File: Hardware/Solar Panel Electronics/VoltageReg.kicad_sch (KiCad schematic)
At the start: 22 parts, among them J14 Screw_Terminal_5VRail, Q2 Q_NMOS_DGS, Q3 Q_NMOS_DGS, U6 LM5118MH, U7 LT1963AxST-3.3

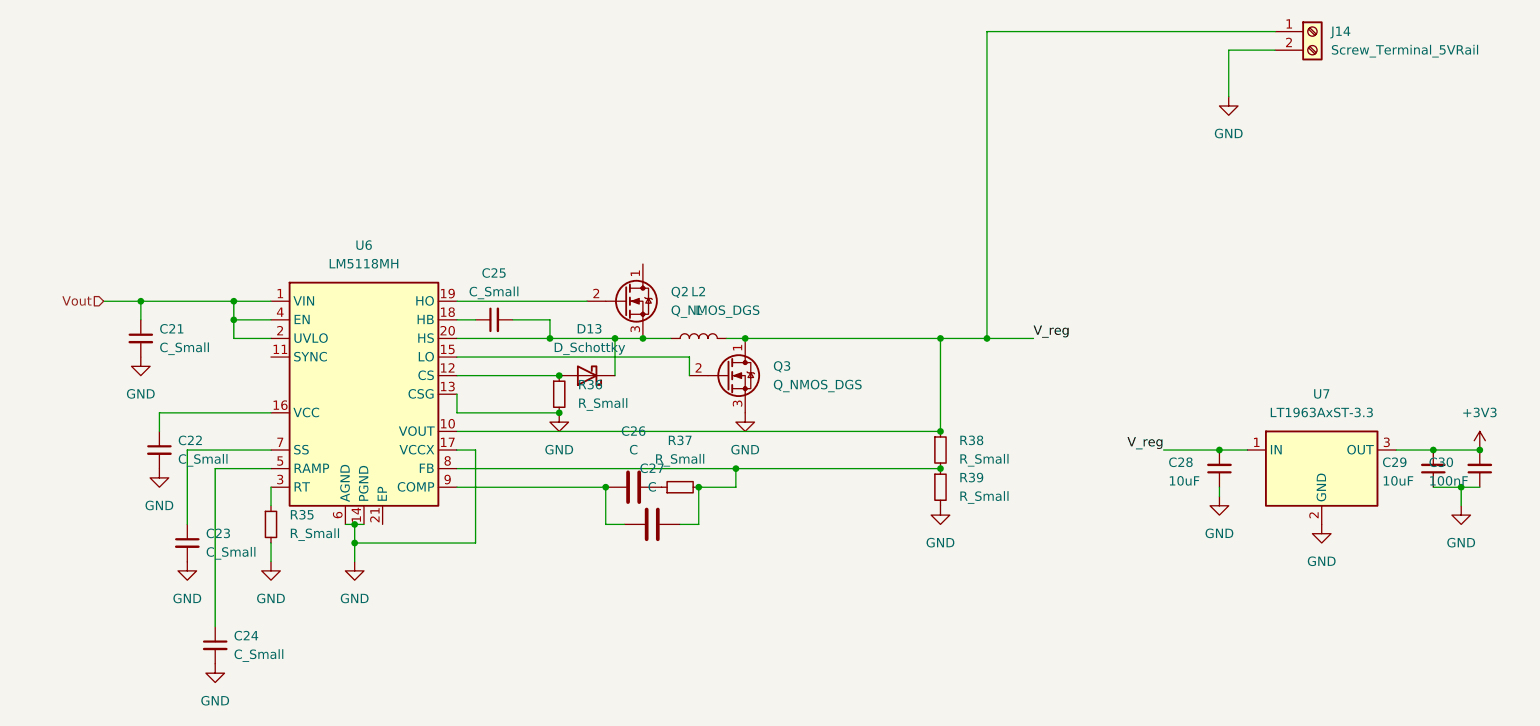
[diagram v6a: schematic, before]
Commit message: Sized the buck-boost converter components. Need to complete pcb layout.
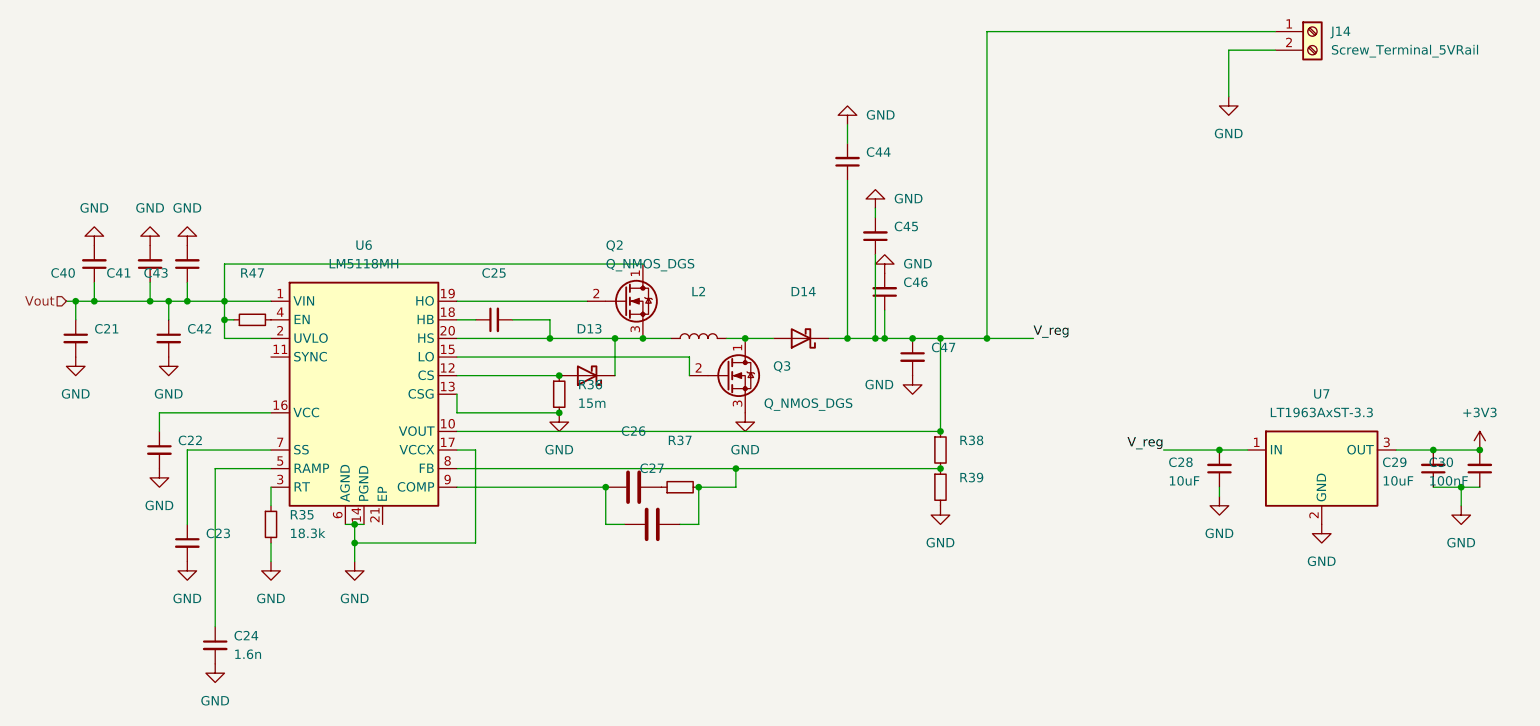
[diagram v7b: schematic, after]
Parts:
- added C40, C41, C42, C43, C44, C45, C46, C47: (no value), Capacitor_SMD:C_0603_1608Metric, symbol Device:C_Small
- added D14: (no value), Diode_SMD:D_SOD-128, symbol Device:D_Schottky
- added R47: (no value), Resistor_SMD:R_0603_1608Metric, symbol Device:R_Small
- C21, C22, C23, C25: value C_Small -> (none)
- C24: value C_Small -> 1.6n
- C26, C27: value C -> (none)
- D13: value D_Schottky -> (none)
- L2: value L -> (none)
- R35: value R_Small -> 18.3k
- R36: value R_Small -> 15m
- R37, R38, R39: value R_Small -> (none)
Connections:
- net GND: now also C40.2, C41.2, C42.2, C43.2, C44.2, C45.2, C46.2, C47.2
- net V_reg: now also C44.1, C45.1, C46.1, C47.1, D14.1 (K); no longer L2.2, Q3.1 (D)
- net Vout: now also Q2.1 (D), C40.1, C41.1, C42.1, C43.1, R47.1; no longer U6.4 (EN)
- new net: D14.2 (A), L2.2, Q3.1 (D)
- new net: R47.2, U6.4 (EN)
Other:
- moved on the sheet: C21

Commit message: Fixed an error in sizing of feedback resistors and capacitors
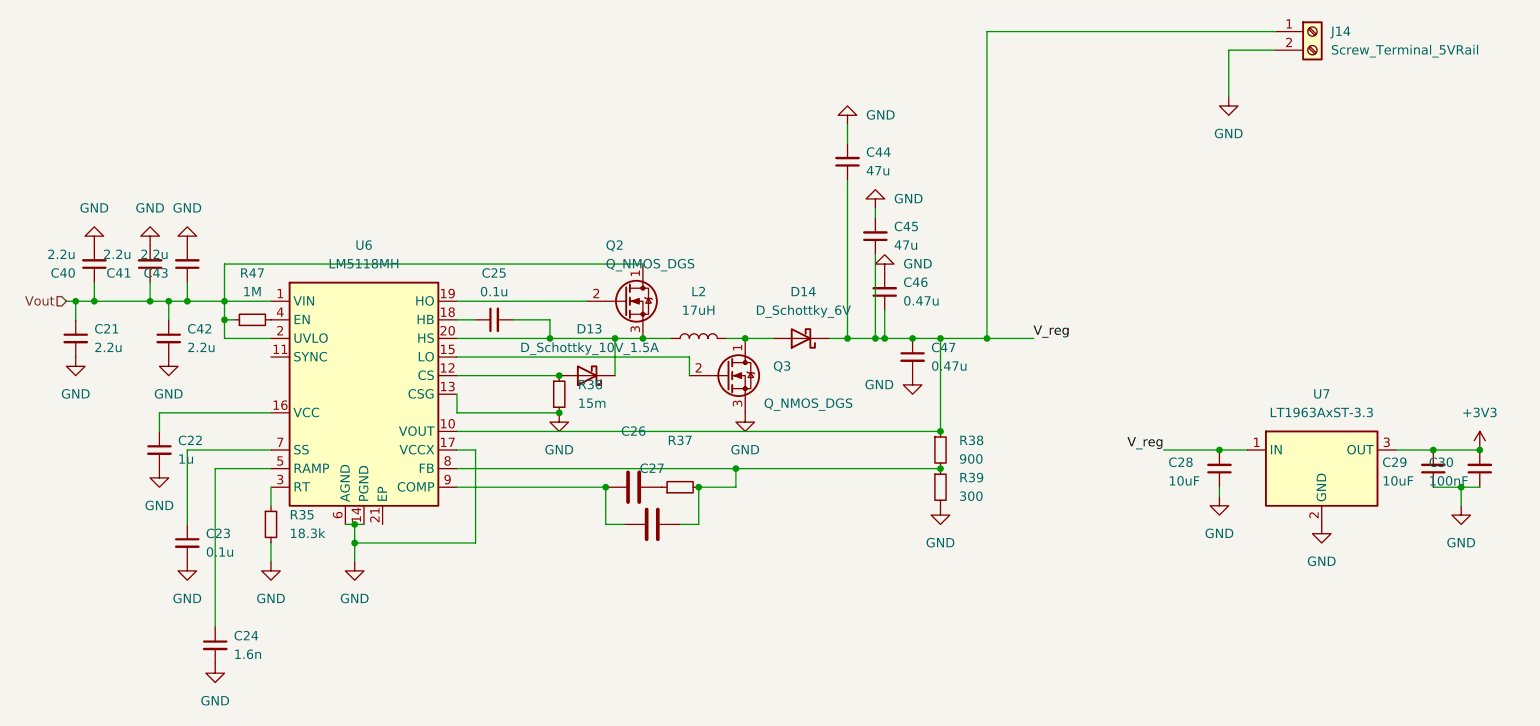
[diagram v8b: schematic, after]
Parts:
- C21, C40, C41, C42, C43: value (none) -> 2.2u
- C22: value (none) -> 1u
- C23, C25: value (none) -> 0.1u
- C44, C45: value (none) -> 47u
- C46, C47: value (none) -> 0.47u
- D13: value (none) -> D_Schottky_10V_1.5A
- D14: value (none) -> D_Schottky_6V
- L2: value (none) -> 17uH
- R38: value (none) -> 900
- R39: value (none) -> 300
- R47: value (none) -> 1M
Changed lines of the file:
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@@
       (effects (font (size 1.27 1.27)) (justify left))
     )
-    (property "Value" "" (id 1) (at 31.75 92.7162 0)
+    (property "Value" "1u" (id 1) (at 31.75 92.7162 0)
       (effects (font (size 1.27 1.27)) (justify left))
     )
@@
       (effects (font (size 1.27 1.27)) (justify left))
     )
-    (property "Value" "" (id 1) (at 134.62 80.0162 0)
+    (property "Value" "0.47u" (id 1) (at 134.62 80.0162 0)
       (effects (font (size 1.27 1.27)) (justify left))
     )
@@
       (effects (font (size 1.27 1.27)) (justify left))
     )
-    (property "Value" "" (id 1) (at 20.32 77.4762 0)
+    (property "Value" "2.2u" (id 1) (at 20.32 77.4762 0)
       (effects (font (size 1.27 1.27)) (justify left))
     )
@@
     (in_bom yes) (on_board yes) (fields_autoplaced)
     (property "Reference" "D13" (id 0) (at 87.9475 74.93 0))
-    (property "Value" "" (id 1) (at 87.9475 77.47 0))
+    (property "Value" "D_Schottky_10V_1.5A" (id 1) (at 87.9475 77.47 0))
     (property "Footprint" "Diode_SMD:D_SOD-128" (id 2) (at 87.63 81.28 0)
       (effects (font (size 1.27 1.27)) hide)
@@
     (in_bom yes) (on_board yes) (fields_autoplaced)
     (property "Reference" "R47" (id 0) (at 41.91 67.31 90))
-    (property "Value" "" (id 1) (at 41.91 69.85 90))
+    (property "Value" "1M" (id 1) (at 41.91 69.85 90))
     (property "Footprint" "Resistor_SMD:R_0603_1608Metric" (id 2) (at 41.91 73.66 0)
       (effects (font (size 1.27 1.27)) hide)
@@
     (in_bom yes) (on_board yes) (fields_autoplaced)
     (property "Reference" "C25" (id 0) (at 74.9363 67.31 90))
-    (property "Value" "" (id 1) (at 74.9363 69.85 90))
+    (property "Value" "0.1u" (id 1) (at 74.9363 69.85 90))
     (property "Footprint" "Capacitor_SMD:C_0603_1608Metric" (id 2) (at 74.93 73.66 0)
       (effects (font (size 1.27 1.27)) hide)
@@
       (effects (font (size 1.27 1.27)) (justify left))
     )
-    (property "Value" "" (id 1) (at 33.02 77.4762 0)
+    (property "Value" "2.2u" (id 1) (at 33.02 77.4762 0)
       (effects (font (size 1.27 1.27)) (justify left))
     )
@@
       (effects (font (size 1.27 1.27)) (justify left))
     )
-    (property "Value" "" (id 1) (at 138.43 97.7899 0)
+    (property "Value" "300" (id 1) (at 138.43 97.7899 0)
       (effects (font (size 1.27 1.27)) (justify left))
     )
@@
       (effects (font (size 1.27 1.27)) (justify right))
     )
-    (property "Value" "" (id 1) (at 125.73 53.3335 0)
+    (property "Value" "47u" (id 1) (at 125.73 53.3335 0)
       (effects (font (size 1.27 1.27)) (justify right))
     )
@@
       (effects (font (size 1.27 1.27)) (justify left))
     )
-    (property "Value" "" (id 1) (at 17.78 64.7638 0)
+    (property "Value" "2.2u" (id 1) (at 17.78 64.7638 0)
       (effects (font (size 1.27 1.27)) (justify left))
     )
@@
       (effects (font (size 1.27 1.27)) (justify left))
     )
-    (property "Value" "" (id 1) (at 35.56 105.4162 0)
+    (property "Value" "0.1u" (id 1) (at 35.56 105.4162 0)
       (effects (font (size 1.27 1.27)) (justify left))
     )
@@
     (in_bom yes) (on_board yes)
     (property "Reference" "D14" (id 0) (at 117.1575 69.85 0))
-    (property "Value" "" (id 1) (at 117.1575 72.39 0))
+    (property "Value" "D_Schottky_6V" (id 1) (at 117.1575 72.39 0))
     (property "Footprint" "Diode_SMD:D_SOD-128" (id 2) (at 116.84 76.2 0)
       (effects (font (size 1.27 1.27)) hide)
@@
       (effects (font (size 1.27 1.27)) (justify left))
     )
-    (property "Value" "" (id 1) (at 138.43 92.7099 0)
+    (property "Value" "900" (id 1) (at 138.43 92.7099 0)
       (effects (font (size 1.27 1.27)) (justify left))
     )
@@
       (effects (font (size 1.27 1.27)) (justify left))
     )
-    (property "Value" "" (id 1) (at 30.48 64.7638 0)
+    (property "Value" "2.2u" (id 1) (at 30.48 64.7638 0)
       (effects (font (size 1.27 1.27)) (justify left))
     )
@@
       (effects (font (size 1.27 1.27)) (justify right))
     )
-    (property "Value" "" (id 1) (at 129.54 63.4935 0)
+    (property "Value" "47u" (id 1) (at 129.54 63.4935 0)
       (effects (font (size 1.27 1.27)) (justify right))
     )
@@
     (in_bom yes) (on_board yes) (fields_autoplaced)
     (property "Reference" "L2" (id 0) (at 102.87 69.85 90))
-    (property "Value" "" (id 1) (at 102.87 72.39 90))
+    (property "Value" "17uH" (id 1) (at 102.87 72.39 90))
     (property "Footprint" "Inductor_SMD:L_0603_1608Metric" (id 2) (at 102.87 76.2 0)
       (effects (font (size 1.27 1.27)) hide)
@@
       (effects (font (size 1.27 1.27)) (justify right))
     )
-    (property "Value" "" (id 1) (at 130.81 71.1135 0)
+    (property "Value" "0.47u" (id 1) (at 130.81 71.1135 0)
       (effects (font (size 1.27 1.27)) (justify right))
     )
@@
       (effects (font (size 1.27 1.27)) (justify left))
     )
-    (property "Value" "" (id 1) (at 25.4 64.7638 0)
-      (effects (font (size 1.27 1.27)) (justify left))
-    )
+    (property "Value" "2.2u" (id 1) (at 25.4 64.7638 0)
+      (effects (font (size 1.27 1.27)) (justify left))
+    )
